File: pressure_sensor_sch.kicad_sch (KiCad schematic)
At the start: 63 parts, among them J13 1053131104, U7 ADS131M06IPBS

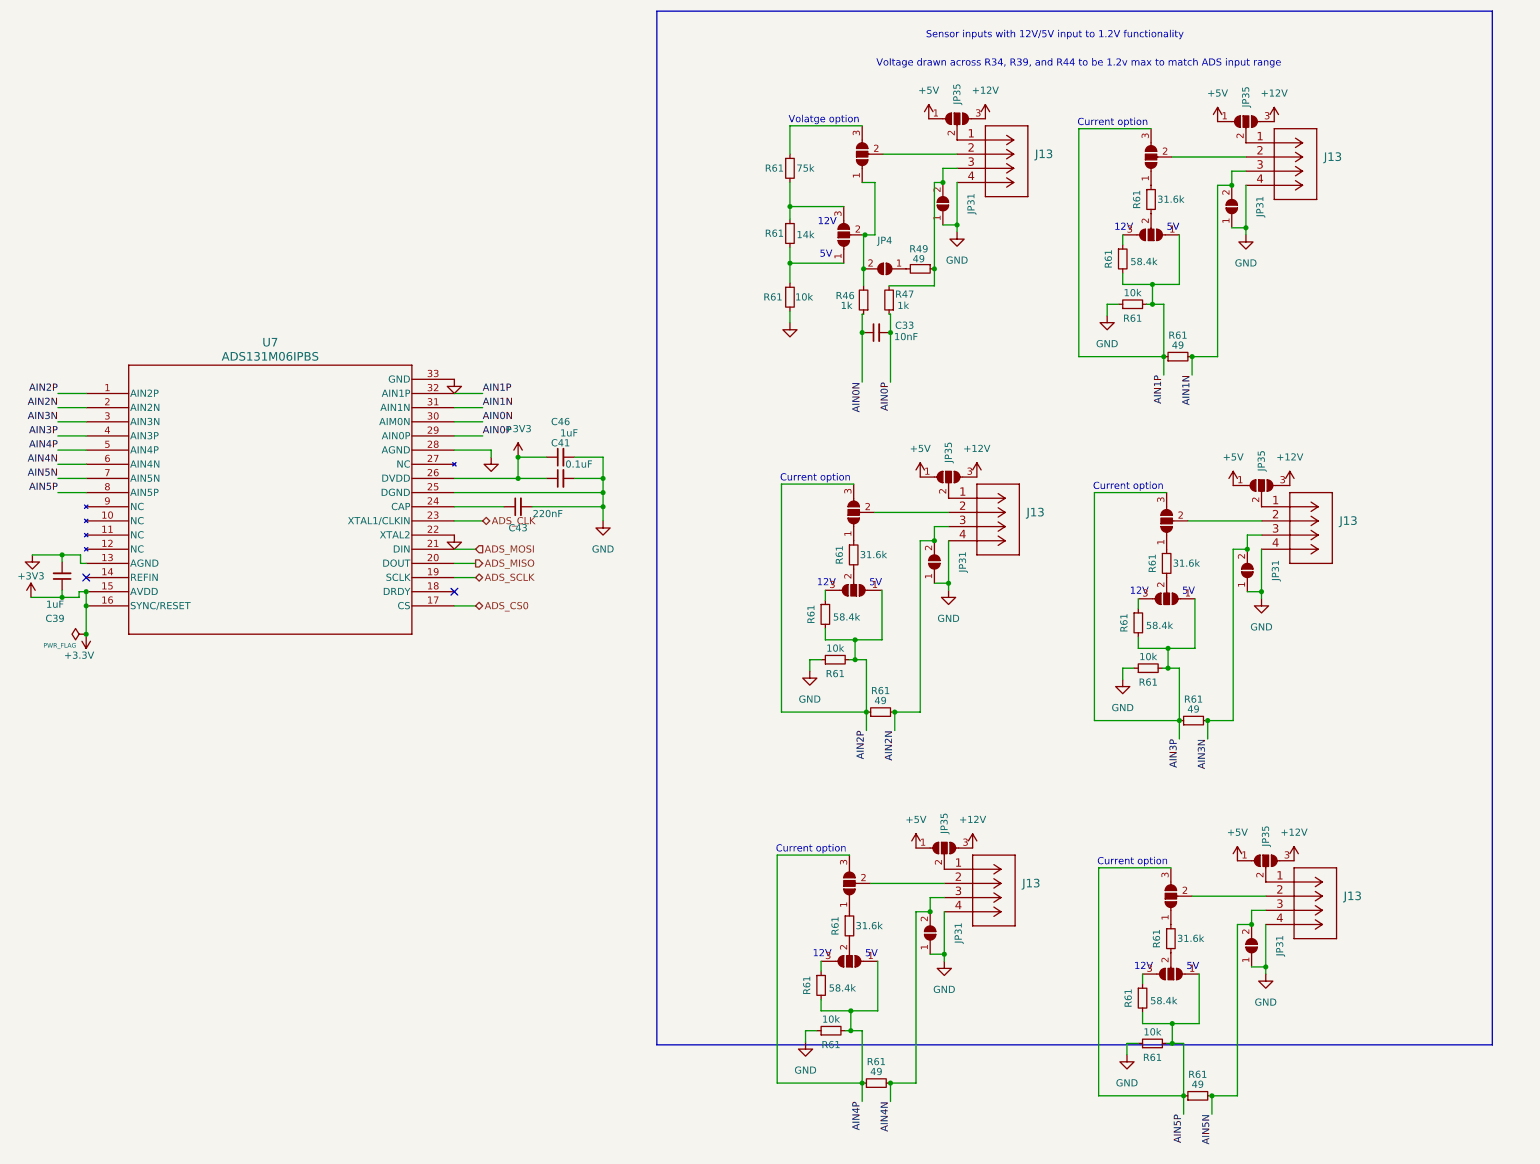
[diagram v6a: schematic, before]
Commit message: reshuffled layout
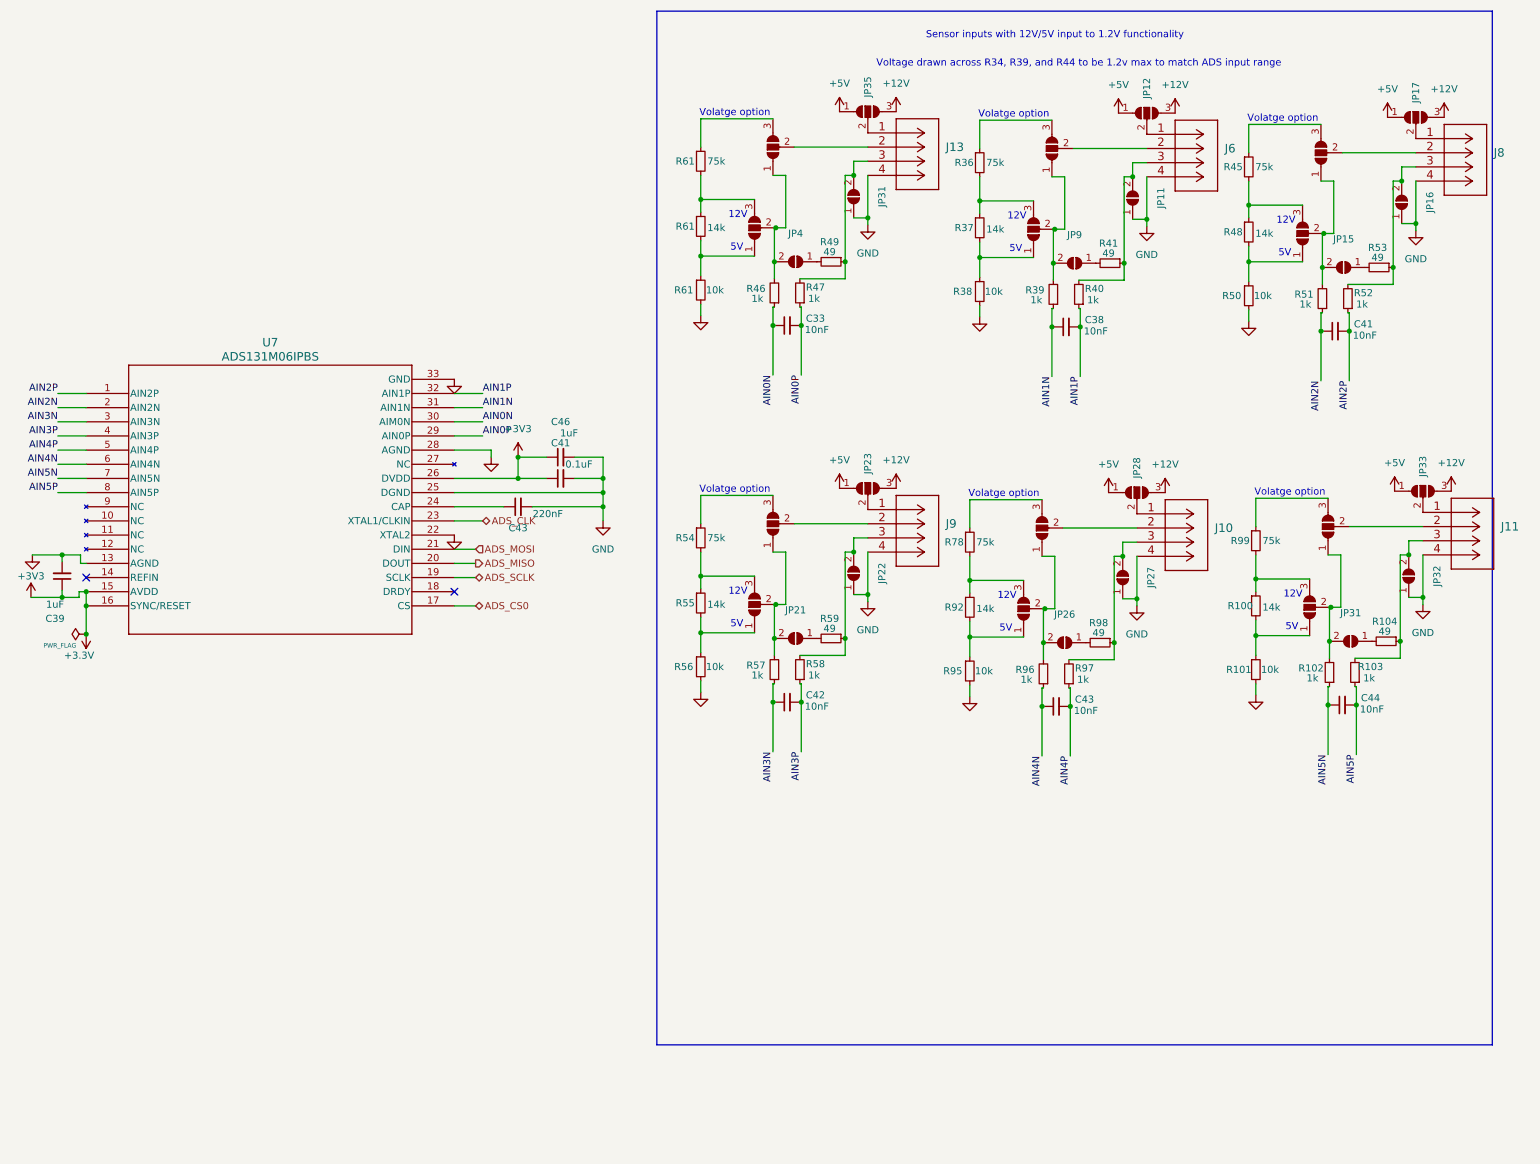
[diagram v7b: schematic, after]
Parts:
- removed J13 (x5): 1053131104, Connector_Molex:Molex_Nano-Fit_105313-xx04_1x04_P2.50mm_Horizontal, symbol iclr:1053131104
- removed JP31 (x5): SolderJumper_2_Open, iclr:SmallerSolderJP, symbol Jumper:SolderJumper_2_Open
- removed JP35 (x5), JP39 (x10): SolderJumper_3_Open, Jumper:SolderJumper-3_P1.3mm_Open_RoundedPad1.0x1.5mm_NumberLabels, symbol Jumper:SolderJumper_3_Open
- removed R61 (x5): 31.6k, Resistor_SMD:R_0402_1005Metric, symbol Device:R_Small
- removed R61 (x5): 58.4k, Resistor_SMD:R_0402_1005Metric, symbol Device:R_Small
- removed R61 (x5): 49, Resistor_SMD:R_0402_1005Metric, symbol Device:R_Small
- removed R61 (x5): 10k, Resistor_SMD:R_0402_1005Metric, symbol Device:R_Small
- added C38, C41, C42, C43, C44: 10nF, Capacitor_SMD:C_0402_1005Metric, symbol Device:C_Small
- added J10, J11, J6, J8, J9: 1053131104, Connector_Molex:Molex_Nano-Fit_105313-xx04_1x04_P2.50mm_Horizontal, symbol iclr:1053131104
- added JP11, JP15, JP16, JP21, JP22, JP26, JP27, JP31, JP32, JP9: SolderJumper_2_Open, iclr:SmallerSolderJP, symbol Jumper:SolderJumper_2_Open
- added JP12, JP13, JP14, JP17, JP18, JP19, JP23, JP24, JP25, JP28, JP29, JP30, JP33, JP6, JP7: SolderJumper_3_Open, Jumper:SolderJumper-3_P1.3mm_Open_RoundedPad1.0x1.5mm_NumberLabels, symbol Jumper:SolderJumper_3_Open
- added R100, R37, R48, R55, R92: 14k, Resistor_SMD:R_0402_1005Metric, symbol Device:R_Small
- added R101, R38, R50, R56, R95: 10k, Resistor_SMD:R_0402_1005Metric, symbol Device:R_Small
- added R102, R103, R39, R40, R51, R52, R57, R58, R96, R97: 1k, Resistor_SMD:R_0402_1005Metric, symbol Device:R_Small
- added R104, R41, R53, R59, R98: 49, Resistor_SMD:R_0402_1005Metric, symbol Device:R_Small
- added R36, R45, R54, R78, R99: 75k, Resistor_SMD:R_0402_1005Metric, symbol Device:R_Small
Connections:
- net +12V: now also JP12.3 (B), JP17.3 (B), JP23.3 (B), JP28.3 (B), JP33.3 (B)
- net +5V: now also JP12.1 (A), JP17.1 (A), JP23.1 (A), JP28.1 (A), JP33.1 (A)
- net AIN1N: now also C38.1, R39.1
- net AIN1P: now also C38.2, R40.1
- net AIN2N: now also C41.1, R51.1
- net AIN2P: now also C41.2, R52.1
- net AIN3N: now also C42.1, R57.1
- net AIN3P: now also C42.2, R58.1
- net AIN4N: now also C43.1, R96.1
- net AIN4P: now also C43.2, R97.1
- net AIN5N: now also C44.1, R102.1
- net AIN5P: now also C44.2, R103.1
- net GND: now also J10.4, J11.4, J6.4, J8.4, J9.4, JP11.1 (A), JP16.1 (A), JP22.1 (A), JP27.1 (A), JP32.1 (A), R101.2, R38.2, R50.2, R56.2, R95.2
- new net: J11.1, JP33.2 (C)
- new net: J11.2, JP30.2 (C)
- new net: J11.3, JP32.2 (B), R103.2, R104.1
- new net: J8.3, JP16.2 (B), R52.2, R53.1
- new net: J6.1, JP12.2 (C)
- new net: J6.3, JP11.2 (B), R40.2, R41.1
- new net: JP9.1 (A), R41.2
- new net: JP18.3 (B), R54.2, R55.1
- new net: JP18.1 (A), R55.2, R56.1
- new net: JP13.3 (B), R45.2, R48.1
- new net: JP13.1 (A), R48.2, R50.1
- new net: JP6.2 (C), JP7.1 (A), JP9.2 (B), R39.2
- new net: J9.1, JP23.2 (C)
- new net: JP19.3 (B), R54.1
- new net: JP25.3 (B), R78.1
- new net: JP24.3 (B), R78.2, R92.1
- new net: J10.1, JP28.2 (C)
- new net: J10.2, JP25.2 (C)
- new net: J10.3, JP27.2 (B), R97.2, R98.1
- new net: JP6.1 (A), R37.2, R38.1
- new net: JP6.3 (B), R36.2, R37.1
- new net: JP31.1 (A), R104.2
- new net: JP30.3 (B), R99.1
- new net: JP29.3 (B), R100.1, R99.2
- new net: JP7.3 (B), R36.1
- new net: JP15.1 (A), R53.2
- new net: JP13.2 (C), JP14.1 (A), JP15.2 (B), R51.2
- new net: JP29.1 (A), R100.2, R101.1
- new net: J9.3, JP22.2 (B), R58.2, R59.1
- new net: JP18.2 (C), JP19.1 (A), JP21.2 (B), R57.2
- new net: JP24.2 (C), JP25.1 (A), JP26.2 (B), R96.2
- new net: JP26.1 (A), R98.2
- new net: J8.1, JP17.2 (C)
- new net: J6.2, JP7.2 (C)
- new net: JP29.2 (C), JP30.1 (A), JP31.2 (B), R102.2
- new net: J8.2, JP14.2 (C)
- new net: JP14.3 (B), R45.1
- new net: J9.2, JP19.2 (C)
- new net: JP24.1 (A), R92.2, R95.1
- new net: JP21.1 (A), R59.2
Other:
- note removed: "Current option"
- moved on the sheet: C33, J13, JP31, JP35, JP4, R46, R47, R49, R61

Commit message: Added sensors
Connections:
- net AIN0N: now also C38.1, R39.1; no longer C33.1, R46.1
- net AIN0P: now also C38.2, R40.1; no longer C33.2, R47.1
- net AIN1N: now also C33.1, R46.1; no longer C38.1, R39.1
- net AIN1P: now also C33.2, R47.1; no longer C38.2, R40.1
- net AIN2N: now also C42.1, R57.1; no longer C41.1, R51.1
- net AIN2P: now also C42.2, R58.1; no longer C41.2, R52.1
- net AIN3N: now also C41.1, R51.1; no longer C42.1, R57.1
- net AIN3P: now also C41.2, R52.1; no longer C42.2, R58.1
- net AIN4N: now also C44.1, R102.1; no longer C43.1, R96.1
- net AIN4P: now also C44.2, R103.1; no longer C43.2, R97.1
- net AIN5N: now also C43.1, R96.1; no longer C44.1, R102.1
- net AIN5P: now also C43.2, R97.1; no longer C44.2, R103.1
- net at J11.2: now also JP25.2 (C); no longer JP30.2 (C)
- net at JP32.2 (B), R103.2, R104.1: now also J10.3; no longer J11.3
- net at JP16.2 (B), R52.2, R53.1: now also J9.3; no longer J8.3
- net at J10.2: now also JP30.2 (C); no longer JP25.2 (C)
- net at JP27.2 (B), R97.2, R98.1: now also J11.3; no longer J10.3
- net at JP22.2 (B), R58.2, R59.1: now also J8.3; no longer J9.3
- net at JP14.2 (C): now also J9.2; no longer J8.2
- net at JP19.2 (C): now also J8.2; no longer J9.2
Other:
- moved on the sheet: J10, J11, J8, J9, JP17, JP23, JP28, JP33
